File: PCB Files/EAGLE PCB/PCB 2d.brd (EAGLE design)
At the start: 45 x 75 mm, 17 parts

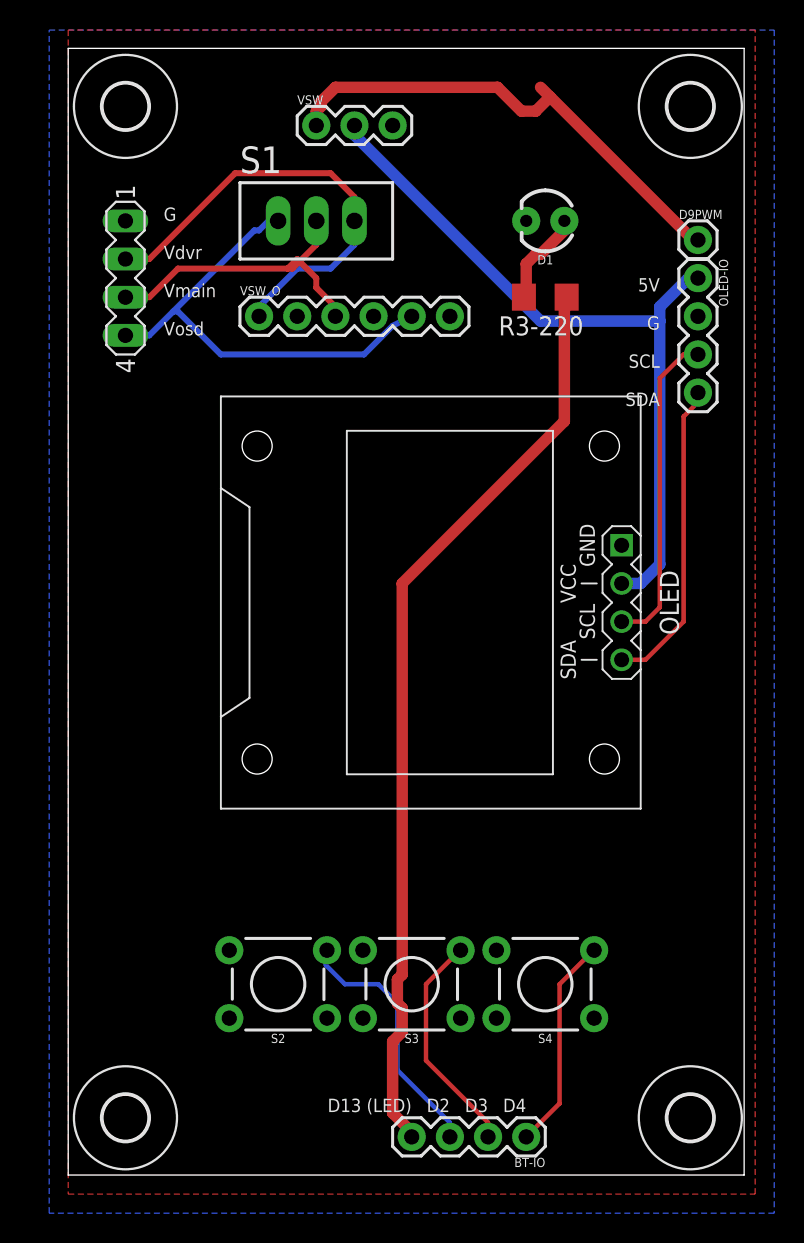
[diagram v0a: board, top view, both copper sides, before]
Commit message: Updated PCBs
• Round edges
• Covered vias on PCB1
• OLED pin swap (VCC <> GND) on PCB2
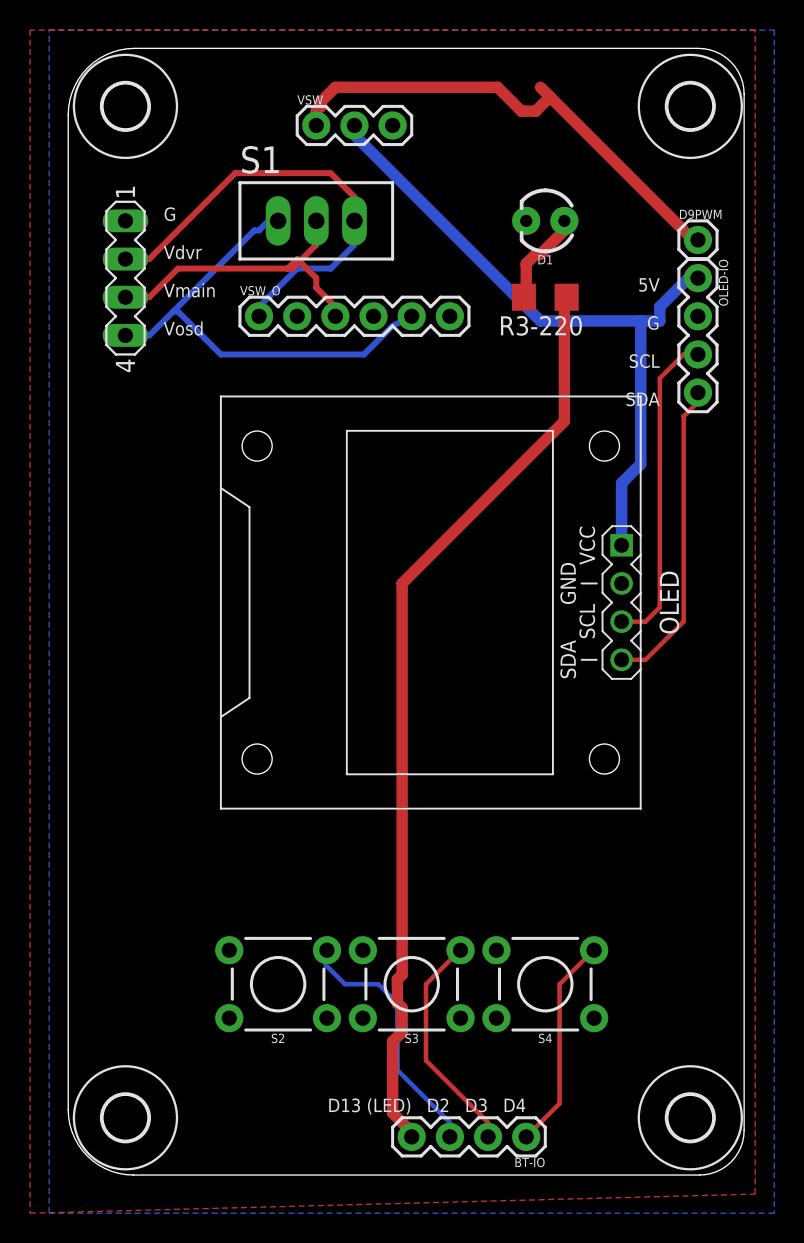
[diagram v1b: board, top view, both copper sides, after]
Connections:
- net GND: now also OLED.2; no longer OLED.1
- net N$4: now also OLED.1; no longer OLED.2
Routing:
- net N$4: track 49.6 -> 45.8 mm
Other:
- outline, holes or cut-outs redrawn

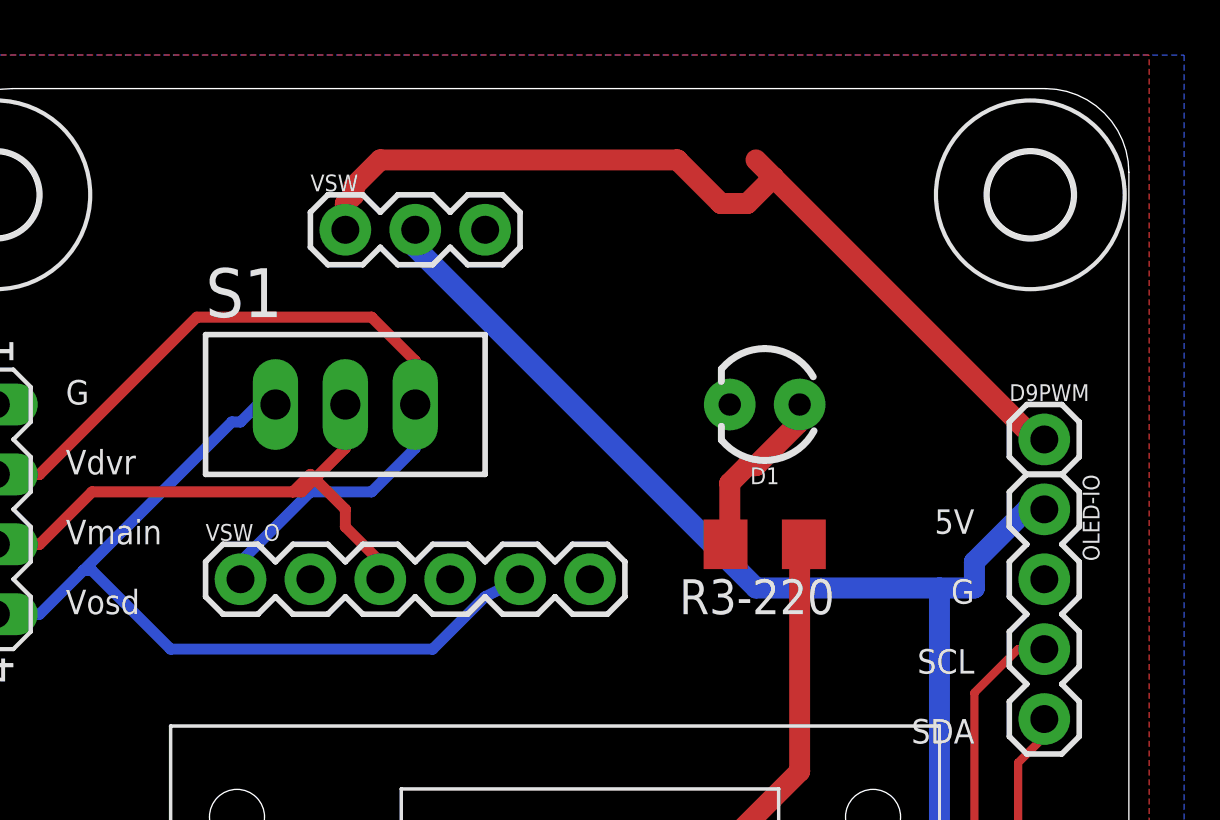
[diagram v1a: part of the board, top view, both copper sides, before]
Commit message: New PCB revision (added a cap)
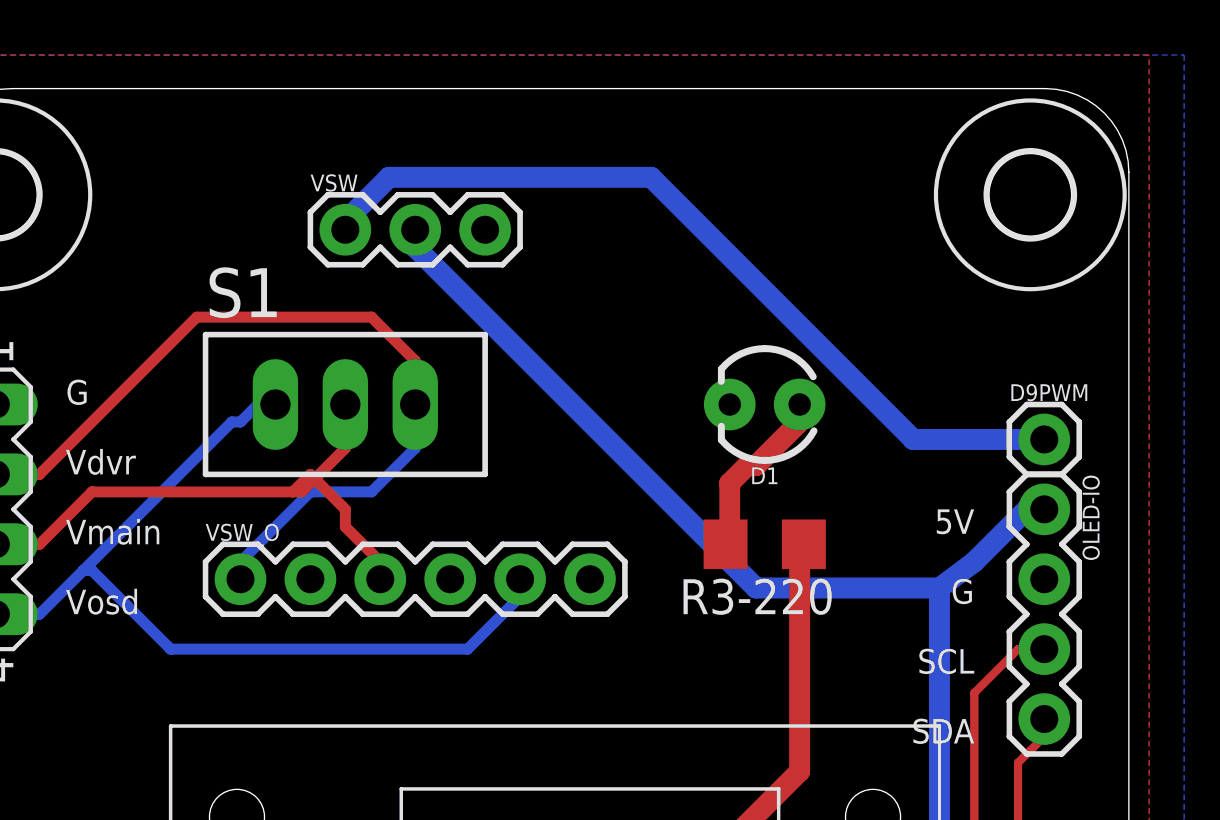
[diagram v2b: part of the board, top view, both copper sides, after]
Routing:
- net N$8: track 33.1 -> 30.6 mm
- net N$4: track 45.8 -> 45.2 mm
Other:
- board text added: "POCKET-GROUNDSTATION | PCB2 | REV2"
- board text removed: "POCKET-GROUNDSTATION | PCB2 | REV1"
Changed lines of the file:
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@@
 <text x="27.94" y="5.08" size="0.889" layer="25" rot="R180">D3</text>
 <text x="30.48" y="5.08" size="0.889" layer="25" rot="R180">D4</text>
-<text x="3.81" y="50.8" size="1.27" layer="26" rot="MR270">POCKET-GROUNDSTATION | PCB2 | REV1</text>
+<text x="3.81" y="50.8" size="1.27" layer="26" rot="MR270">POCKET-GROUNDSTATION | PCB2 | REV2</text>
 <text x="6.35" y="63.5" size="0.889" layer="25">G</text>
 <text x="6.35" y="60.96" size="0.889" layer="25">Vdvr</text>
@@
 <wire x1="13.97" y1="63.5" x2="13.335" y2="63.5" width="0.4" layer="16" locked="yes"/>
 <contactref element="VSW_O" pad="5"/>
-<wire x1="21.59" y1="56.515" x2="22.86" y2="57.15" width="0.4" layer="16" locked="yes"/>
-<wire x1="19.685" y1="54.61" x2="21.59" y2="56.515" width="0.4" layer="16" locked="yes"/>
-<wire x1="10.16" y1="54.61" x2="19.685" y2="54.61" width="0.4" layer="16" locked="yes"/>
+<wire x1="22.86" y1="56.515" x2="22.86" y2="57.15" width="0.4" layer="16"/>
+<wire x1="20.955" y1="54.61" x2="22.86" y2="56.515" width="0.4" layer="16"/>
+<wire x1="10.16" y1="54.61" x2="20.955" y2="54.61" width="0.4" layer="16"/>
 <wire x1="7.3025" y1="57.4675" x2="10.16" y2="54.61" width="0.4" layer="16" locked="yes"/>
 <wire x1="6.985" y1="57.4675" x2="7.3025" y2="57.4675" width="0.4" layer="16" locked="yes"/>
@@
 <signal name="N$4">
 <contactref element="OLED-IO" pad="1"/>
-<wire x1="39.37" y1="57.785" x2="39.37" y2="56.8325" width="0.762" layer="16" locked="yes"/>
+<wire x1="39.37" y1="57.785" x2="38.1" y2="56.8325" width="0.762" layer="16"/>
 <wire x1="41.275" y1="59.69" x2="39.37" y2="57.785" width="0.762" layer="16" locked="yes"/>
 <wire x1="41.91" y1="59.69" x2="41.275" y2="59.69" width="0.762" layer="16" locked="yes"/>
@@
 <wire x1="19.05" y1="69.215" x2="19.05" y2="69.85" width="0.762" layer="16" locked="yes"/>
 <wire x1="31.4325" y1="56.8325" x2="19.05" y2="69.215" width="0.762" layer="16" locked="yes"/>
-<wire x1="39.37" y1="56.8325" x2="38.1" y2="56.8325" width="0.762" layer="16" locked="yes"/>
 <contactref element="OLED" pad="1"/>
 <wire x1="38.1" y1="56.8325" x2="31.4325" y2="56.8325" width="0.762" layer="16" locked="yes"/>
@@
 <contactref element="VSW" pad="1"/>
 <contactref element="D9PWM" pad="1"/>
-<wire x1="41.5925" y1="62.23" x2="32.0675" y2="71.755" width="0.762" layer="1" locked="yes"/>
-<wire x1="32.0675" y1="71.755" x2="31.4325" y2="72.39" width="0.762" layer="1" locked="yes"/>
 <wire x1="41.91" y1="62.23" x2="41.5925" y2="62.23" width="0.762" layer="1" locked="yes"/>
-<wire x1="16.51" y1="70.8025" x2="16.51" y2="69.85" width="0.762" layer="1" locked="yes"/>
-<wire x1="16.8275" y1="71.12" x2="16.51" y2="70.8025" width="0.762" layer="1" locked="yes"/>
-<wire x1="16.8275" y1="71.4375" x2="16.8275" y2="71.12" width="0.762" layer="1" locked="yes"/>
-<wire x1="17.78" y1="72.39" x2="16.8275" y2="71.4375" width="0.762" layer="1" locked="yes"/>
-<wire x1="28.575" y1="72.39" x2="17.78" y2="72.39" width="0.762" layer="1" locked="yes"/>
-<wire x1="30.1625" y1="70.8025" x2="28.575" y2="72.39" width="0.762" layer="1" locked="yes"/>
-<wire x1="31.115" y1="70.8025" x2="30.1625" y2="70.8025" width="0.762" layer="1" locked="yes"/>
-<wire x1="32.0675" y1="71.755" x2="31.115" y2="70.8025" width="0.762" layer="1" locked="yes"/>
+<wire x1="37.1475" y1="62.23" x2="41.91" y2="62.23" width="0.762" layer="16"/>
+<wire x1="27.6225" y1="71.755" x2="37.1475" y2="62.23" width="0.762" layer="16"/>
+<wire x1="18.0975" y1="71.755" x2="27.6225" y2="71.755" width="0.762" layer="16"/>
+<wire x1="16.51" y1="70.1675" x2="18.0975" y2="71.755" width="0.762" layer="16"/>
+<wire x1="16.51" y1="69.85" x2="16.51" y2="70.1675" width="0.762" layer="16"/>
 </signal>
 </signals>
